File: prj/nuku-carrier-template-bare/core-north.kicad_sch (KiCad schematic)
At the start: 1 part, among them J4 DF40HC(4.0)-90DS-0.4V

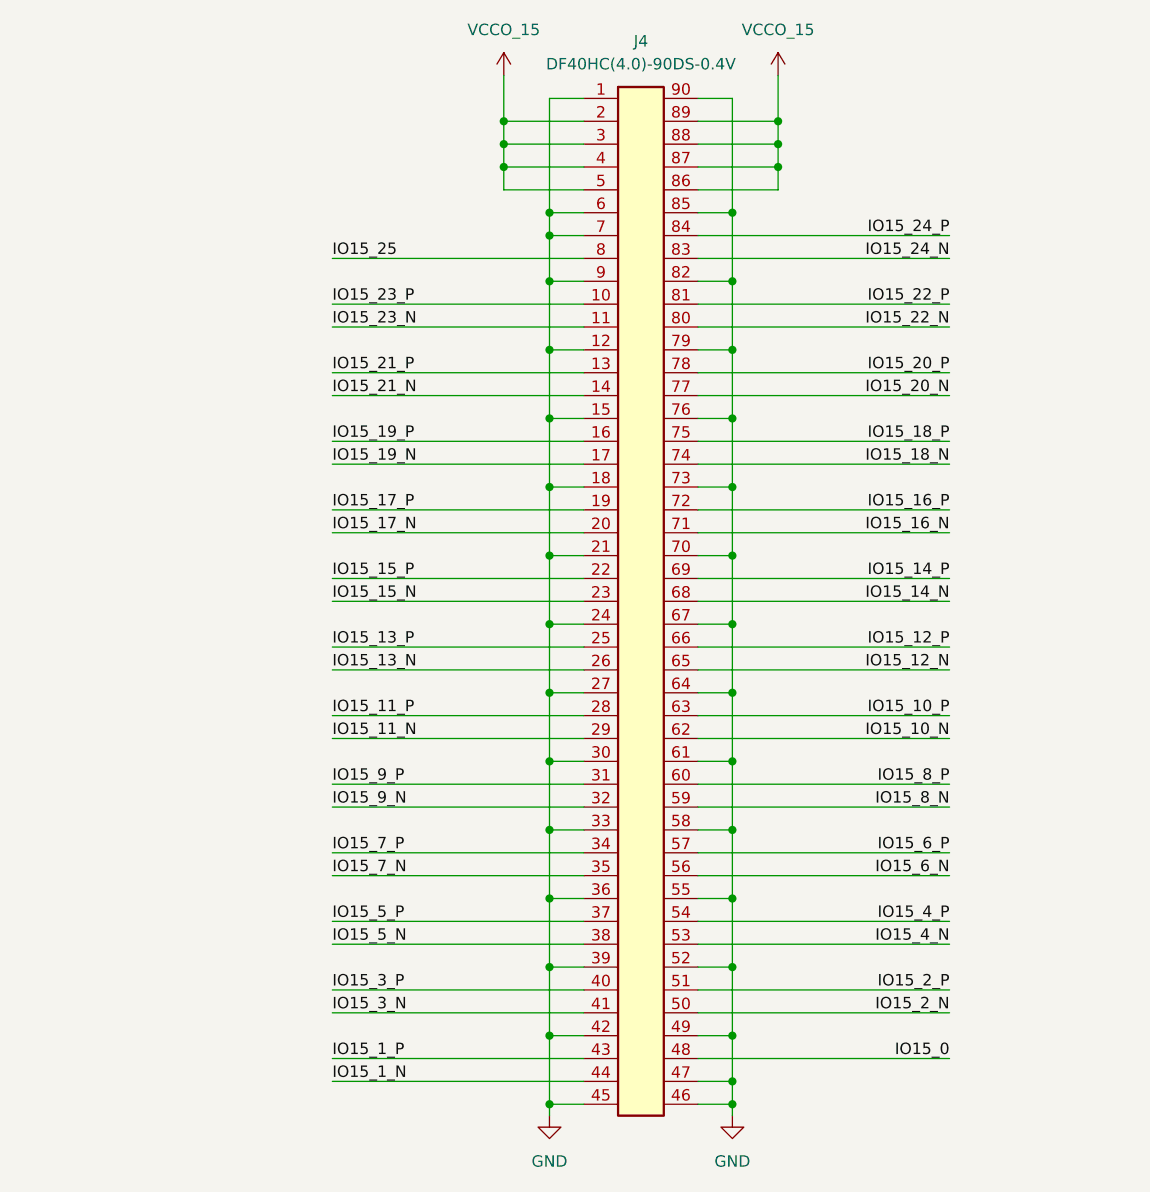
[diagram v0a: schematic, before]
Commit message: Update nuku.carrier.template to template.bare
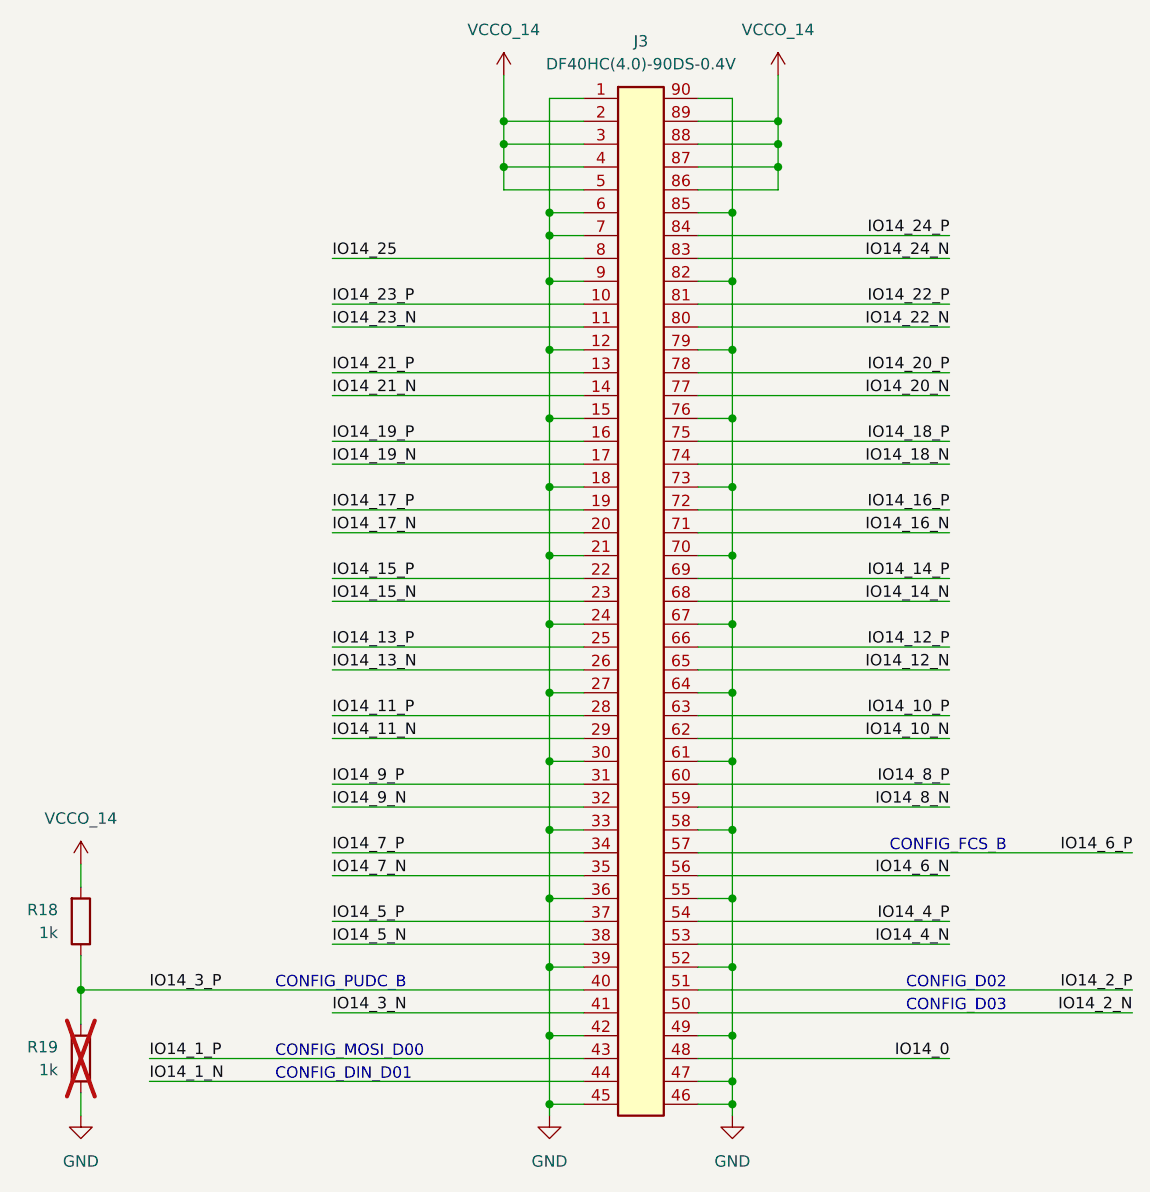
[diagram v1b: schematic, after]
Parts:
- removed J4: DF40HC(4.0)-90DS-0.4V, nuku:DF40HC(4.0)-90DS-0.4V, symbol nuku:DF40HC(4.0)-90DS-0.4V
- added J3: DF40HC(4.0)-90DS-0.4V, nuku:DF40HC(4.0)-90DS-0.4V, symbol nuku:DF40HC(4.0)-90DS-0.4V
- added R18, R19: 1k, Resistor_SMD:R_0402_1005Metric, symbol Device:R
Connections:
- net GND: now also J3.1, J3.12, J3.15, J3.18, J3.21, J3.24, J3.27, J3.30, J3.33, J3.36, J3.39, J3.42, J3.45, J3.46, J3.47, J3.49, J3.52, J3.55, J3.58, J3.6, J3.61, J3.64, J3.67, J3.7, J3.70, J3.73, J3.76, J3.79, J3.82, J3.85, J3.9, J3.90, R19.1
- new net IO14_0: J3.48
- new net IO14_10_N: J3.62
- new net IO14_10_P: J3.63
- new net IO14_11_N: J3.29
- new net IO14_11_P: J3.28
- new net IO14_12_N: J3.65
- new net IO14_12_P: J3.66
- new net IO14_13_N: J3.26
- new net IO14_13_P: J3.25
- new net IO14_14_N: J3.68
- new net IO14_14_P: J3.69
- new net IO14_15_N: J3.23
- new net IO14_15_P: J3.22
- new net IO14_16_N: J3.71
- new net IO14_16_P: J3.72
- new net IO14_17_N: J3.20
- new net IO14_17_P: J3.19
- new net IO14_18_N: J3.74
- new net IO14_18_P: J3.75
- new net IO14_19_N: J3.17
- new net IO14_19_P: J3.16
- new net IO14_1_N: J3.44
- new net IO14_1_P: J3.43
- new net IO14_20_N: J3.77
- new net IO14_20_P: J3.78
- new net IO14_21_N: J3.14
- new net IO14_21_P: J3.13
- new net IO14_22_N: J3.80
- new net IO14_22_P: J3.81
- new net IO14_23_N: J3.11
- new net IO14_23_P: J3.10
- new net IO14_24_N: J3.83
- new net IO14_24_P: J3.84
- new net IO14_25: J3.8
- new net IO14_2_N: J3.50
- new net IO14_2_P: J3.51
- new net IO14_3_N: J3.41
- new net IO14_3_P: J3.40, R18.1, R19.2
- new net IO14_4_N: J3.53
- new net IO14_4_P: J3.54
- new net IO14_5_N: J3.38
- new net IO14_5_P: J3.37
- new net IO14_6_N: J3.56
- new net IO14_6_P: J3.57
- new net IO14_7_N: J3.35
- new net IO14_7_P: J3.34
- new net IO14_8_N: J3.59
- new net IO14_8_P: J3.60
- new net IO14_9_N: J3.32
- new net IO14_9_P: J3.31
- new net VCCO_14: J3.2, J3.3, J3.4, J3.5, J3.86, J3.87, J3.88, J3.89, R18.2
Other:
- note added: "CONFIG_D02"
- note added: "CONFIG_D03"
- note added: "CONFIG_DIN_D01"
- note added: "CONFIG_FCS_B"
- note added: "CONFIG_MOSI_D00"
- note added: "CONFIG_PUDC_B"
- company: (none) -> Samuel López Asunción
- title: (none) -> nuku.carrier.template.bare / core-north-14

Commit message: Route template.basic
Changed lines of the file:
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@@
 	(text "CONFIG_PUDC_B"
 		(exclude_from_sim no)
-		(at 107.95 139.7 0)
+		(at 93.98 139.7 0)
 		(effects
 			(font
@@
 	)
 	(label "IO14_3_P"
-		(at 93.98 139.7 0)
-		(effects
-			(font
+		(at 114.3 139.7 0)
+		(effects
+			(font
